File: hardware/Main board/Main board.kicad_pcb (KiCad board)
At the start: 2 copper layers, 100 parts, among them J1 Wind Direction, J10 Free Pins, J11 Nokia 5110 LCD, J2 Wind Speed, J3 USB_B_Micro, J4 Micro_SD_Card, J5 Sensor board connector, J6 Barrel_Jack, J7 ISP programmer, J8 SPI1, J9 SPI2, Q1 IRLML2060, Q1 Q_PNP_BCE, SW1 SW_Push, SW2 SW_SPST, SW3 SW_Push, SW4 SW_Push, SW5 Page Switch btn, SW6 LCD rst btn, U1 FT232RL, U2 MCP6042, U3 SCWN03A-03, U4 ATmega1284P-AU, U5 DS3231MZ, U6 ENC28J60, U7 USB6B1, U8 DRV5053, Y1 16MHZ

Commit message: Updated main board
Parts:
- removed the Q1 at (136.7, 116.8)
- removed R11: 100k, Resistor_SMD:R_0805_2012Metric
- removed R11: 330K, Resistor_SMD:R_0805_2012Metric
- moved D6 205.7 mm to (16.8, 75.5)
- moved BT1 203.8 mm to (52.2, 74.2), turned to 180 degrees
- moved D4 202.9 mm to (16.8, 68.0)
- moved D5 193.3 mm to (16.8, 71.8)
- moved C14 191.4 mm to (19.8, 87.0), turned to 180 degrees
- moved R25 187.5 mm to (21.2, 83.0)
- moved D7 185.2 mm to (16.8, 79.2)
- moved U5 183.0 mm to (60.0, 74.6)
- moved D8 179.6 mm to (16.8, 83.0)
- moved R24 179.3 mm to (21.2, 79.2)
- moved C16 176.5 mm to (27.2, 26.0)
- moved R9 172.1 mm to (60.9, 81.8), turned to 180 degrees
- moved R22 165.3 mm to (21.2, 71.8)
- moved R23 159.7 mm to (21.2, 75.5)
- moved R21 152.5 mm to (21.3, 68.0)
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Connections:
- R10 pad 1: +3V3 -> VCC
- R9 pad 2: +3V3 -> VCC
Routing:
- net VCC: track 329.7 -> 668.6 mm, vias 0 -> 3
- net SCK: track 69.3 -> 261.1 mm
- net MISO: track 65.0 -> 231.3 mm
- net MOSI: track 61.6 -> 213.9 mm
- net /ETHER_CS: track 0.00 -> 127.8 mm, vias 0 -> 2
- net PC2: track 0.00 -> 99.5 mm, vias 0 -> 3
- net PA6: track 0.00 -> 82.2 mm, vias 0 -> 1
- net /SD_CS: track 0.00 -> 80.1 mm, vias 0 -> 2
- net PA5: track 0.00 -> 76.9 mm, vias 0 -> 1
- net PC5: track 0.00 -> 73.5 mm, vias 0 -> 1
- net Net-(R25-Pad2): track 0.00 -> 73.0 mm, vias 0 -> 2
- net PA4: track 0.00 -> 71.5 mm, vias 0 -> 1
- net PA3: track 0.00 -> 69.3 mm, vias 0 -> 1
- net Net-(R24-Pad2): track 0.00 -> 69.2 mm, vias 0 -> 2
- net Net-(R23-Pad2): track 0.00 -> 68.5 mm, vias 0 -> 2
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
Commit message: Finished the board design
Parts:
- added D11: PWR_LED, Diode_SMD:D_0805_2012Metric, F.Cu at (237.7, 38.8)
- added MNT1: MountingHole_3mm_Pad, MountingHole:MountingHole_3mm_Pad, F.Cu at (239.9, 15.3)
- added MNT2: MountingHole_3mm_Pad, MountingHole:MountingHole_3mm_Pad, F.Cu at (238.0, 103.1)
- added MNT3: MountingHole_3mm_Pad, MountingHole:MountingHole_3mm_Pad, F.Cu at (16.8, 103.0)
- added MNT4: MountingHole_3mm_Pad, MountingHole:MountingHole_3mm_Pad, F.Cu at (17.0, 29.0)
- added R11: 100k, Resistor_SMD:R_0805_2012Metric, F.Cu at (168.5, 102.6)
- added R34: 55, Resistor_SMD:R_0805_2012Metric, F.Cu at (237.7, 43.2)
- added TP1: WindDir, Meteo_Footprints:Test_Pad, F.Cu at (80.8, 42.8)
- added TP2: WindSpeed, Meteo_Footprints:Test_Pad, F.Cu at (90.8, 46.2)
- BT1: footprint Battery:BatteryHolder_Keystone_103_1x20mm -> Battery:BatteryHolder_Keystone_106_1x20mm
- J10: footprint TerminalBlock_Phoenix:TerminalBlock_Phoenix_MKDS-1,5-6_1x06_P5.00mm_Horizontal -> TerminalBlock_Phoenix:TerminalBlock_Phoenix_MKDS-1,5-8_1x08_P5.00mm_Horizontal
- J11: footprint Connector_PinHeader_2.54mm:PinHeader_1x08_P2.54mm_Vertical -> Meteo_Footprints:Nokia_5110_LCD
- J3: footprint Connector_USB:USB_Micro-B_Molex-105017-0001 -> Meteo_Footprints:KYCON_KMMVX-SMT-BS-BTR
- U8: footprint Package_TO_SOT_THT:TO-92 -> Connector_PinSocket_2.54mm:PinSocket_1x03_P2.54mm_Vertical
- moved Q1 127.7 mm to (172.0, 102.5), turned to 180 degrees
- moved R33 126.9 mm to (175.5, 102.4), turned to 270 degrees
- moved J11 107.8 mm to (146.0, 100.0), turned to 0 degrees
- moved J4 32.3 mm to (53.5, 96.0)
- moved C14 30.8 mm to (50.5, 85.8)
- moved U6 7.50 mm to (195.0, 28.8)
- moved C15 7.50 mm to (210.0, 29.2)
- moved C12 4.85 mm to (61.0, 79.2), turned to 0 degrees
- moved R10 1.50 mm to (60.9, 81.2)
- moved R9 1.50 mm to (60.9, 83.2)
- moved BT1 1.35 mm to (52.8, 75.5)
- moved C3 0.89 mm to (32.2, 52.8)
- moved J3 0.79 mm to (18.0, 52.2), turned to 90 degrees
- moved R2 0.38 mm to (71.0, 29.8)
- moved R3 0.38 mm to (66.0, 29.8)
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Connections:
- C18 pad 1: GND -> Net-(C17-Pad2)
- C18 pad 2: Net-(C17-Pad2) -> GND
- J10 pad 6: (no net) -> GND
- U7 pad 2: Net-(J3-Pad2) -> Net-(J3-Pad3)
- U7 pad 3: Net-(J3-Pad3) -> Net-(J3-Pad2)
- U7 pad 6: Net-(U1-Pad15) -> Net-(U1-Pad16)
- U7 pad 7: Net-(U1-Pad16) -> Net-(U1-Pad15)
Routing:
- net MOSI: track 213.9 -> 359.1 mm, vias 1 -> 3
- net SCK: track 261.1 -> 402.6 mm, vias 1 -> 5
- net PD7: track 0.00 -> 117.9 mm, vias 0 -> 2
- net VCC: track 668.6 -> 753.6 mm, vias 3 -> 8
- net MISO: track 231.3 -> 287.6 mm, vias 1 -> 3
- net Net-(C24-Pad1): track 62.4 -> 96.6 mm
- net PC3: track 63.8 -> 80.2 mm
- net /SD_CS: track 80.1 -> 64.6 mm
- net PC5: track 73.5 -> 83.1 mm
- net /ETHER_CS: track 127.8 -> 135.7 mm
- net Net-(Q1-Pad1): track 0.00 -> 7.05 mm
- net PB0: track 52.2 -> 59.1 mm, vias 1 -> 3
- net Net-(J11-Pad7): track 0.00 -> 4.76 mm
- net dirOUT: track 25.1 -> 28.4 mm
- net Net-(D11-Pad2): track 0.00 -> 2.55 mm
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- added copper zone on B.Cu, net GND
- added copper zone on F.Cu, net GND
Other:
- board text added: "12V"
- board text added: "3V3"
- board text added: "3V3 PWR"
- board text added: "BMP_CS"
- board text added: "Ethernet Activity"
- board text added: "GND"
- board text added: "HIH_CS"
- board text added: "MISO"
- board text added: "MOSI"
- board text added: "Motherboard for meteorological station v0.1 by Daniels Fišers"
- board text added: "PA3"
- board text added: "PA4"
- board text added: "PA5"
- board text added: "PA6"
- board text added: "PA7"
- board text added: "PB0"
- board text added: "PC2"
- board text added: "PIN1"
- board text added: "Power"
- board text added: "RXLED"
- board text added: "Reading data"
- board text added: "SCK"
- board text added: "SPI1"
- board text added: "SPI2"
- board text added: "Sensor Board Connector"
- board text added: "SpeedOut"
- board text added: "Startup"
- board text added: "TXLED"
- board text added: "VCC"
- board text added: "Wind Direction Connector"
- board text added: "Wind Speed"
- board text added: "WindDirOut"
- board text added: "Write to SD card"

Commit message: Added 0 new easter eggs
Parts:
- added C25: 4.7uF, Capacitor_SMD:CP_Elec_4x5.4, F.Cu at (229.0, 42.0)
- C18: footprint Capacitor_SMD:C_0805_2012Metric_Pad1.15x1.40mm_HandSolder -> Capacitor_SMD:CP_Elec_4x5.3
- SW1, SW3, SW4, SW5, SW6: footprint Button_Switch_SMD:SW_SPST_B3S-1100 -> Button_Switch_SMD:SW_Push_1P1T_NO_6x6mm_H9.5mm
- Y1: footprint Crystal:Crystal_SMD_EuroQuartz_MT-4Pin_3.2x2.5mm -> Meteo_Footprints:Crystal_SMD
- moved J5 254.4 mm to (254.0, 115.0), turned to 180 degrees
- moved MNT4 246.7 mm to (252.5, 102.5), turned to 180 degrees
- moved MNT3 244.6 mm to (252.5, 37.5), turned to 180 degrees
- moved D8 240.4 mm to (255.2, 52.0), turned to 180 degrees
- moved D7 239.5 mm to (255.2, 55.8), turned to 180 degrees
- moved D6 238.9 mm to (255.2, 59.5), turned to 180 degrees
- moved D5 238.5 mm to (255.2, 63.2), turned to 180 degrees
- moved D4 238.4 mm to (255.2, 67.0), turned to 180 degrees
- moved J3 238.0 mm to (254.0, 82.8), turned to 270 degrees
- moved C16 232.6 mm to (244.8, 108.8), turned to 180 degrees
- moved R25 231.6 mm to (250.8, 52.0), turned to 180 degrees
- moved R24 230.7 mm to (250.8, 55.8), turned to 180 degrees
- moved R23 230.1 mm to (250.8, 59.5), turned to 180 degrees
- moved C2 230.0 mm to (249.2, 87.5), turned to 90 degrees
- moved R22 229.7 mm to (250.8, 63.2), turned to 180 degrees
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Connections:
- J4 pad 9: Net-(J4-Pad9) -> GND
- Y1 pad 2: Net-(C8-Pad2) -> GND
- Y1 pad 3: (no net) -> Net-(C8-Pad2)
- Y1 pad 4: (no net) -> GND
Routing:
- net SCK: track 402.6 -> 359.6 mm
- net MOSI: track 359.1 -> 318.7 mm
- net Net-(C24-Pad1): track 96.6 -> 137.0 mm, vias 0 -> 2
- net Net-(J6-Pad2): track 21.5 -> 48.7 mm
- net PD7: track 117.9 -> 95.9 mm, vias 2 -> 6
- net VCC: track 753.6 -> 737.9 mm
- net 12V: track 174.3 -> 158.7 mm
- net GND: track 28.3 -> 13.4 mm
- net PC3: track 80.2 -> 94.2 mm, vias 1 -> 3
- net Net-(J6-Pad1): track 15.3 -> 27.1 mm
- net PC5: track 83.1 -> 89.4 mm, vias 1 -> 4
- net RXD: track 48.3 -> 52.3 mm
- net Net-(J11-Pad7): track 4.76 -> 7.41 mm
- net RST: track 102.4 -> 103.4 mm
- net PC7: track 38.6 -> 39.5 mm
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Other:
- board text added: "Hall sensor"
- board text added: "Motherboard for meteorological station v0.2 by Daniels Fišers"
- board text added: "No easter eggs here"
- board text removed: "Motherboard for meteorological station v0.1 by Daniels Fišers"

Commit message: Added 0 new easter eggs
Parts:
- removed C24: 100nF, Capacitor_SMD:C_0805_2012Metric_Pad1.15x1.40mm_HandSolder
- removed R32: 100k, Resistor_SMD:R_0805_2012Metric
- removed SW6: LCD rst btn, Button_Switch_SMD:SW_Push_1P1T_NO_6x6mm_H9.5mm
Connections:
- J10 pad 5: PC2 -> GND
- J10 pad 6: GND -> VCC
- J11 pad 1: Net-(C24-Pad1) -> PC2
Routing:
- net Net-(C24-Pad1): track 137.0 -> 0.00 mm, vias 2 -> 0
- net VCC: track 737.9 -> 743.2 mm
- net PC2: track 99.5 -> 103.3 mm
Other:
- board text removed: "PC2"

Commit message: Improved the design of the PCB
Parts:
- moved MNT1 20.3 mm to (41.5, 97.8)
- moved MNT4 17.7 mm to (269.5, 97.8)
- moved C14 17.6 mm to (216.0, 43.0), turned to 270 degrees
- moved C25 16.6 mm to (212.5, 43.5), turned to 270 degrees
- moved MNT3 15.9 mm to (268.0, 34.0)
- moved C17 8.86 mm to (246.8, 96.0)
- moved C18 8.86 mm to (242.0, 96.8)
- moved C2 8.86 mm to (251.8, 96.0)
- moved C3 8.86 mm to (242.3, 90.8)
- moved D10 8.86 mm to (244.2, 86.0)
- moved D9 8.86 mm to (244.2, 83.5)
- moved J3 8.86 mm to (256.5, 91.2)
- moved R26 8.86 mm to (248.2, 83.5)
- moved R27 8.86 mm to (248.2, 86.0)
- moved U1 8.86 mm to (235.2, 88.5)
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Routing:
- net /SD_CS: track 65.4 -> 77.3 mm
- net VCC: track 743.2 -> 732.0 mm, vias 8 -> 7
- net TXD: track 49.5 -> 58.4 mm
- net MOSI: track 318.7 -> 326.9 mm, vias 3 -> 1
- net RST: track 103.4 -> 110.5 mm, vias 1 -> 3
- net RXD: track 52.3 -> 59.4 mm, vias 2 -> 4
- net /HIH_CS: track 85.5 -> 89.8 mm, vias 0 -> 1
- net SCK: track 359.6 -> 363.5 mm, vias 5 -> 3
- net MISO: track 288.0 -> 286.0 mm, vias 3 -> 1
- net Net-(BT1-Pad1): track 5.42 -> 6.61 mm

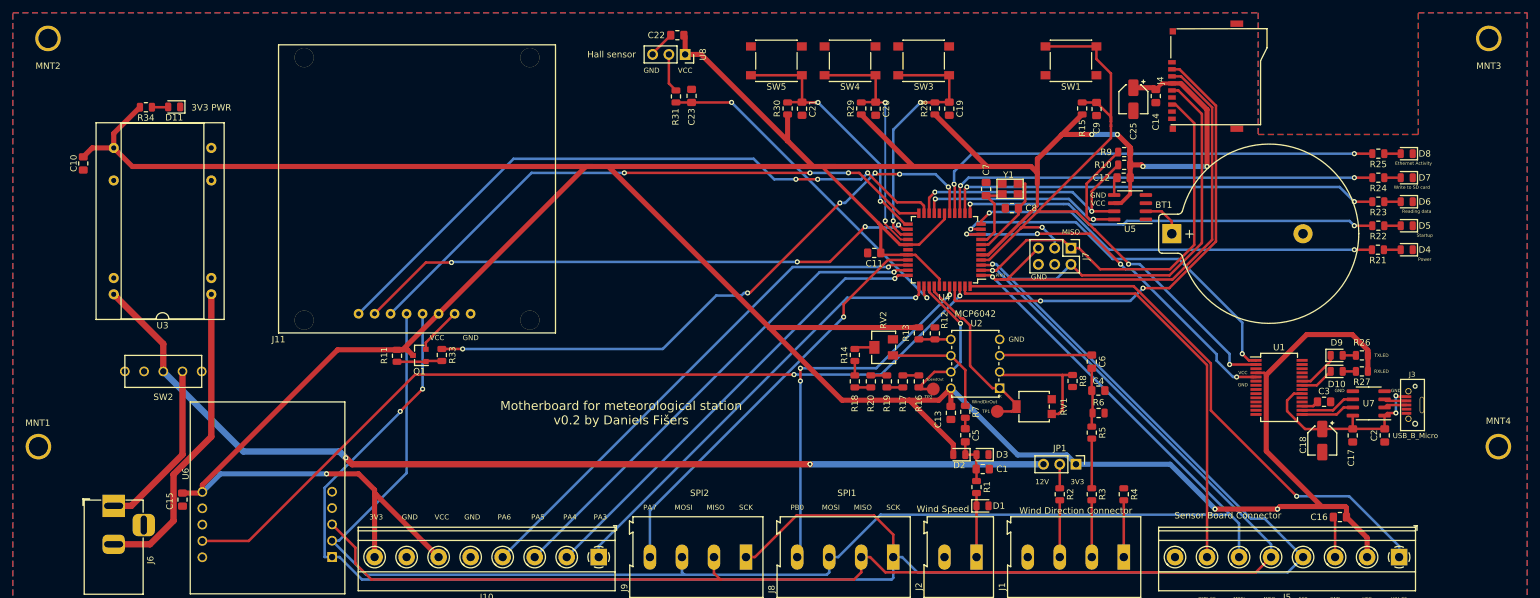
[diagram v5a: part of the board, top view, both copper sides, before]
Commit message: Updated the main board to v0.5
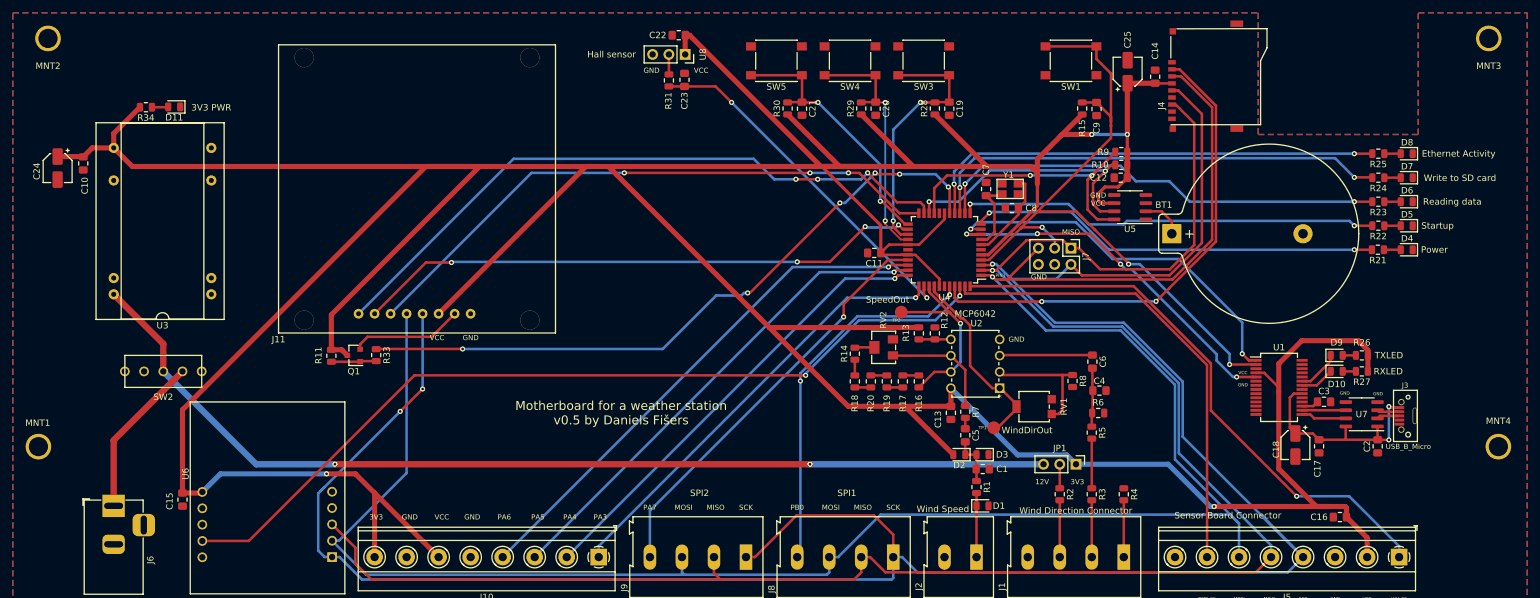
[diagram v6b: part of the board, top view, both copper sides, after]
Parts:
- added C24: 4.7uF, Capacitor_SMD:CP_Elec_4x5.4, F.Cu at (44.5, 54.2)
- moved TP2 13.0 mm to (176.2, 76.8)
- moved R33 10.3 mm to (94.2, 83.5)
- moved Q1 10.2 mm to (90.8, 83.5)
- moved R11 10.2 mm to (87.2, 83.6)
- moved C17 5.52 mm to (241.5, 97.7)
- moved C25 4.39 mm to (211.6, 39.2), turned to 90 degrees
- moved C18 4.26 mm to (237.8, 97.5)
- moved C14 3.03 mm to (215.9, 40.0), turned to 90 degrees
- moved C23 2.73 mm to (142.4, 40.5)
- moved R31 2.73 mm to (140.0, 40.6)
- moved TP1 2.61 mm to (190.7, 94.8)
- moved C2 2.02 mm to (250.7, 97.7)
- moved J3 2.02 mm to (255.4, 93.0)
- moved U7 2.02 mm to (248.2, 92.7)
- moved C12 0.45 mm to (210.5, 55.8)
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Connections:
- J6 pad 2: Net-(J6-Pad2) -> GND
- U3 pad 2: Net-(J6-Pad2) -> GND
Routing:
- net VCC: track 732.0 -> 804.0 mm, vias 7 -> 4
- net Net-(J6-Pad2): track 48.7 -> 0.00 mm
- net SCK: track 363.5 -> 377.1 mm
- net GND: track 13.4 -> 0.56 mm
- net PD7: track 95.6 -> 105.8 mm
- net Net-(J11-Pad7): track 7.41 -> 17.5 mm
- net MOSI: track 326.9 -> 335.2 mm
- net MISO: track 286.0 -> 292.3 mm
- net speedOUT: track 24.4 -> 29.7 mm
- net Net-(R24-Pad2): track 69.2 -> 72.9 mm
- net Net-(R23-Pad2): track 68.5 -> 71.7 mm
- net Net-(R31-Pad1): track 6.08 -> 3.13 mm
- net Net-(R9-Pad1): track 44.9 -> 47.7 mm
- net Net-(C17-Pad2): track 31.4 -> 34.2 mm
- net PA2: track 53.8 -> 55.9 mm
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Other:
- board text added: "Motherboard for a weather station v0.5 by Daniels Fišers"
- board text removed: "Motherboard for meteorological station v0.2 by Daniels Fišers"
